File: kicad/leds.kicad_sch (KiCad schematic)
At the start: 4 parts, among them J1 Conn_01x04, J6 Conn_01x03

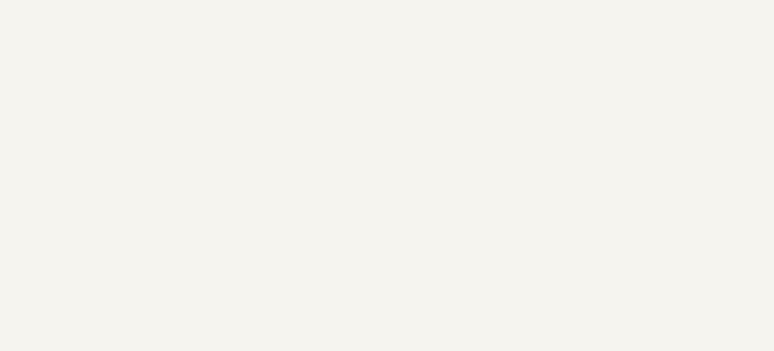
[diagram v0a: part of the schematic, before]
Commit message: Fixed power issue
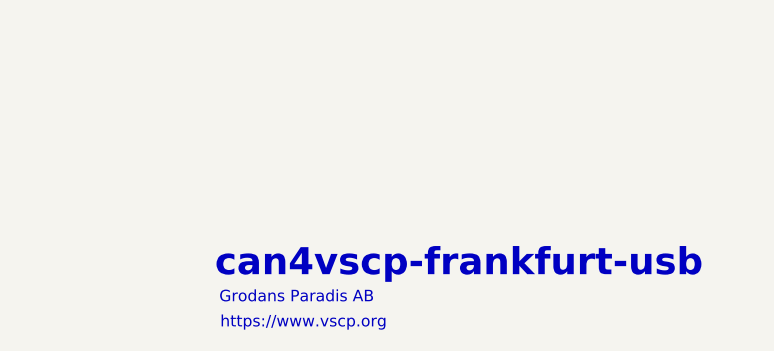
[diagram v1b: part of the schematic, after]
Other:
- note added: "Grodans Paradis AB"
- note added: "can4vscp-frankfurt-usb"
- note added: "https://www.vscp.org"
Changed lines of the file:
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@@
 	(generator_version "10.0")
 	(paper "A4")
+	(text "can4vscp-frankfurt-usb"
+		(exclude_from_sim no)
+		(at 208.788 170.942 0)
+		(effects
+			(font
+				(size 3 3)
+				(thickness 0.6)
+				(bold yes)
+			)
+		)
+	)
+	(text "https://www.vscp.org"
+		(exclude_from_sim no)
+		(at 191.516 177.546 0)
+		(effects
+			(font
+				(size 1.27 1.27)
+			)
+		)
+	)
 	(text "led A == wifi (green)\nled B == status (blue)"
 		(exclude_from_sim no)
@@
 		)
 	)
+	(text "Grodans Paradis AB"
+		(exclude_from_sim no)
+		(at 190.754 174.752 0)
+		(effects
+			(font
+				(size 1.27 1.27)
+			)
+		)
+	)

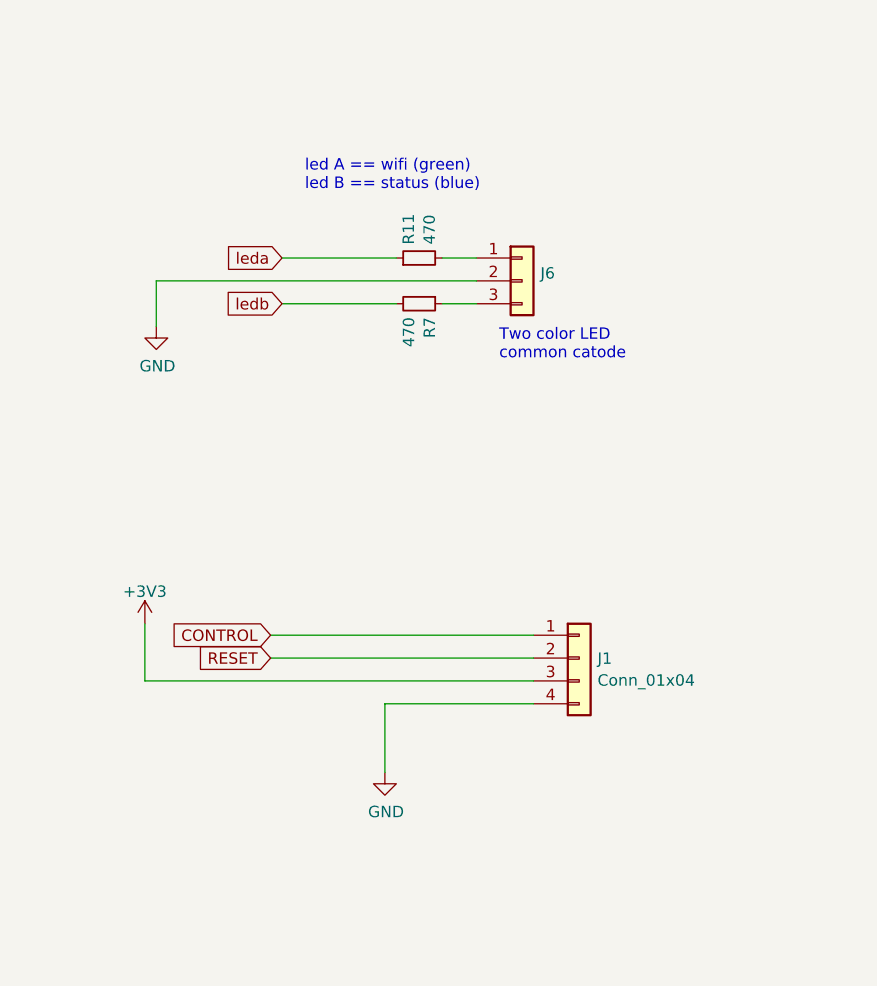
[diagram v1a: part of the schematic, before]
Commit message: Added butons
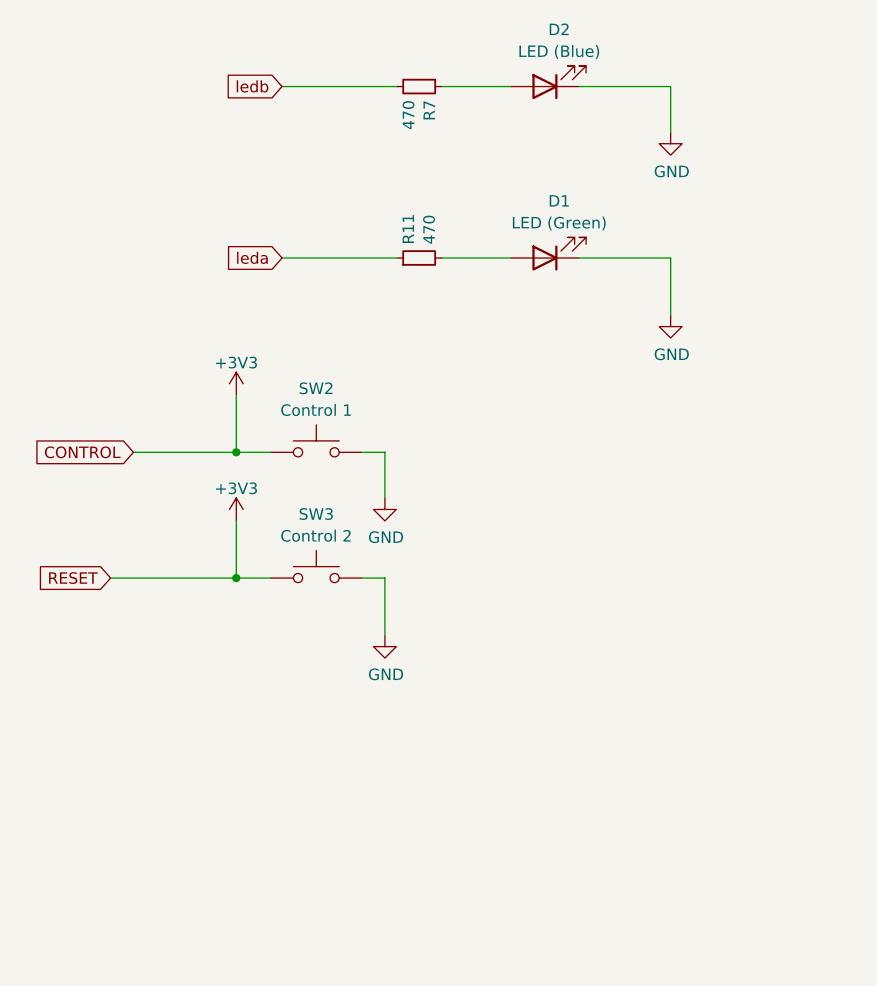
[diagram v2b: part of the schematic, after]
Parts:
- removed J1: Conn_01x04, symbol Connector_Generic:Conn_01x04
- removed J6: Conn_01x03, Connector_PinHeader_2.54mm:PinHeader_1x03_P2.54mm_Vertical, symbol Connector_Generic:Conn_01x03
- added D1: LED (Green), symbol Device:LED
- added D2: LED (Blue), symbol Device:LED
- added SW2: Control 1, Button_Switch_SMD:SW_SPST_Omron_B3FS-100xP, symbol Switch:SW_Omron_B3FS
- added SW3: Control 2, Button_Switch_SMD:SW_SPST_Omron_B3FS-100xP, symbol Switch:SW_Omron_B3FS
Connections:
- net +3V3: now also SW2.1, SW3.1
- net GND: now also D1.1 (K), D2.1 (K), SW2.2, SW3.2
- net at R11.2: now also D1.2 (A)
- net at R7.1: now also D2.2 (A)
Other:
- note removed: "Two color LED common catode"
- note removed: "led A == wifi (green) led B == status (blue)"
- moved on the sheet: R7

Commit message: Reversion A schema and PCB
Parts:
- added R21, R9: 10K, Resistor_SMD:R_0805_2012Metric, symbol Device:R_Small
- D1, D2: footprint (none) -> LED_SMD:LED_0805_2012Metric
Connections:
- net +3V3 renamed CTRL1
- net CTRL1: now also R9.2; no longer SW3.1
- new net +3.3V: R21.1, R9.1
- new net CTRL2: R21.2, SW3.1
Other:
- moved on the sheet: D1, D2, R11, R7, SW2, SW3
